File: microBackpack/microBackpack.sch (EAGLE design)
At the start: 96 parts, among them IC1 LM324D, IC2 LM324D, J2 USB_B, J4 2X6 FEMALE, U1 ATMEGA328P_TQFP, U10 TLP185, U11 TLP185, U2 5VREG-HS, U3 CP2102N-QFN24, U4 TVS_DIODE_4PK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

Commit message: rerouted fgen and crystal as diff pair. Should be better for high frequency
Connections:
- net N$1 renamed CRYS_P
- net N$2 renamed CRYS_N
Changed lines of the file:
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@@
 <?xml version="1.0" encoding="utf-8"?>
 <!DOCTYPE eagle SYSTEM "eagle.dtd">
-<eagle version="9.1.2">
+<eagle version="9.4.2">
 <drawing>
 <settings>
@@
 <class number="0" name="default" width="0" drill="0">
 </class>
+<class number="1" name="crystalDiff" width="0.254" drill="0">
+</class>
 </classes>
 <parts>
@@
 </busses>
 <nets>
-<net name="N$1" class="0">
+<net name="CRYS_P" class="1">
 <segment>
 <pinref part="Q1" gate="G$1" pin="2"/>
@@
 </segment>
 </net>
-<net name="N$2" class="0">
+<net name="CRYS_N" class="1">
 <segment>
 <pinref part="Q1" gate="G$1" pin="1"/>

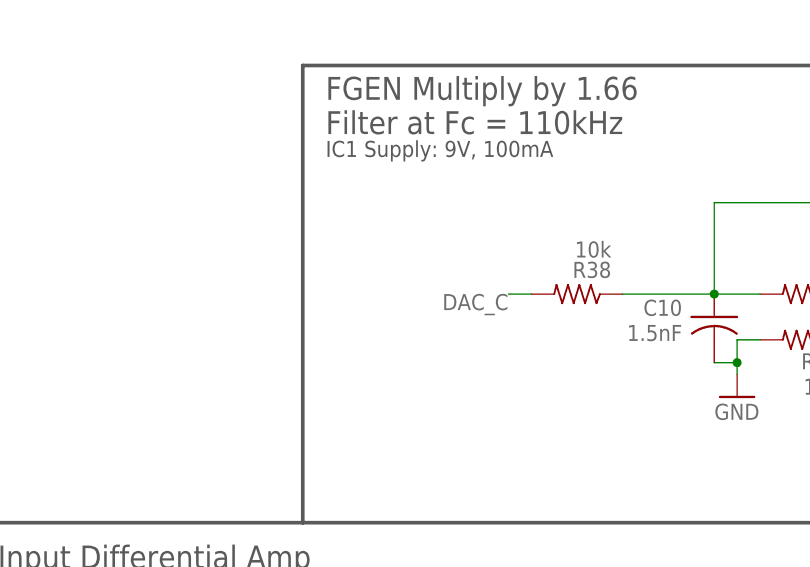
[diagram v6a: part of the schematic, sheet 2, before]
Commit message: Finished routing FGEN, added option for DIO DDS or DAC powered FGEN
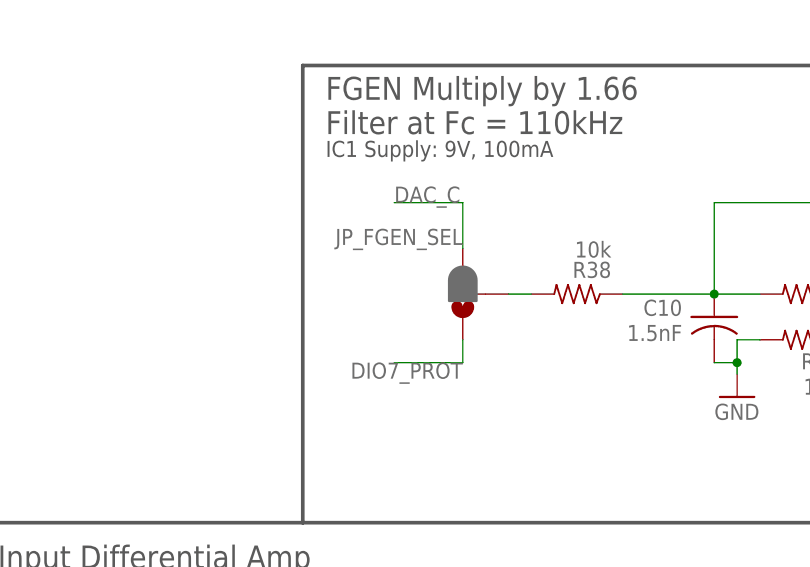
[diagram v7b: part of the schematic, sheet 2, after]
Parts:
- added JP_FGEN_SEL: JUMPER-SMT_3_1-NC_PASTE_SILK, SparkFun-Jumpers:JUMPER-SMT_3_1-NC_PASTE_SILK
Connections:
- new net N$2: JP_FGEN_SEL.2, R38.2
- net DAC_C: now also JP_FGEN_SEL.3; no longer R38.2
- net DIO7_PROT: now also JP_FGEN_SEL.1
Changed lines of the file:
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@@
 <part name="H6" library="holes" library_urn="urn:adsk.eagle:library:237" deviceset="MOUNT-HOLE" device="2.8" package3d_urn="urn:adsk.eagle:package:14271/1"/>
 <part name="J6" library="SparkFun-Connectors" library_urn="urn:adsk.eagle:library:513" deviceset="CONN_05" device="NO_SILK" package3d_urn="urn:adsk.eagle:package:38108/1"/>
+<part name="JP_FGEN_SEL" library="SparkFun-Jumpers" library_urn="urn:adsk.eagle:library:528" deviceset="JUMPER-SMT_3_1-NC_PASTE" device="_SILK" package3d_urn="urn:adsk.eagle:package:39293/1"/>
 </parts>
 <sheets>
@@
 <attribute name="VALUE" x="113.03" y="125.222" size="1.778" layer="96" rot="R180"/>
 </instance>
+<instance part="JP_FGEN_SEL" gate="G$1" x="96.52" y="119.38" smashed="yes" rot="R180">
+<attribute name="NAME" x="96.52" y="126.619" size="1.778" layer="95" font="vector" rot="R180"/>
+</instance>
 </instances>
 <busses>
@@
 </segment>
 <segment>
-<wire x1="101.6" y1="119.38" x2="104.14" y2="119.38" width="0.1524" layer="91"/>
-<label x="101.6" y="119.38" size="1.778" layer="95" rot="R180"/>
-<pinref part="R38" gate="G$1" pin="2"/>
+<pinref part="JP_FGEN_SEL" gate="G$1" pin="3"/>
+<wire x1="96.52" y1="124.46" x2="96.52" y2="129.54" width="0.1524" layer="91"/>
+<wire x1="96.52" y1="129.54" x2="88.9" y2="129.54" width="0.1524" layer="91"/>
+<label x="88.9" y="129.54" size="1.778" layer="95"/>
 </segment>
 </net>
@@
 </segment>
 </net>
+<net name="N$2" class="0">
+<segment>
+<pinref part="JP_FGEN_SEL" gate="G$1" pin="2"/>
+<pinref part="R38" gate="G$1" pin="2"/>
+<wire x1="101.6" y1="119.38" x2="104.14" y2="119.38" width="0.1524" layer="91"/>
+</segment>
+</net>
+<net name="DIO7_PROT" class="0">
+<segment>
+<pinref part="JP_FGEN_SEL" gate="G$1" pin="1"/>
+<wire x1="96.52" y1="114.3" x2="96.52" y2="111.76" width="0.1524" layer="91"/>
+<wire x1="96.52" y1="111.76" x2="88.9" y2="111.76" width="0.1524" layer="91"/>
+<label x="96.52" y="111.76" size="1.778" layer="95" rot="R180"/>
+</segment>
+</net>
